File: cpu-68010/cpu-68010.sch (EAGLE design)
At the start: 47 parts, among them IC10 74HC30D, IC11 74HC30D, IC12 74HC85D, IC13 MAX232, IC6 74HC00D, IC7 74HCT154DW, IC8 74HC04D, IC9 74HC148D, X1 FABC96R

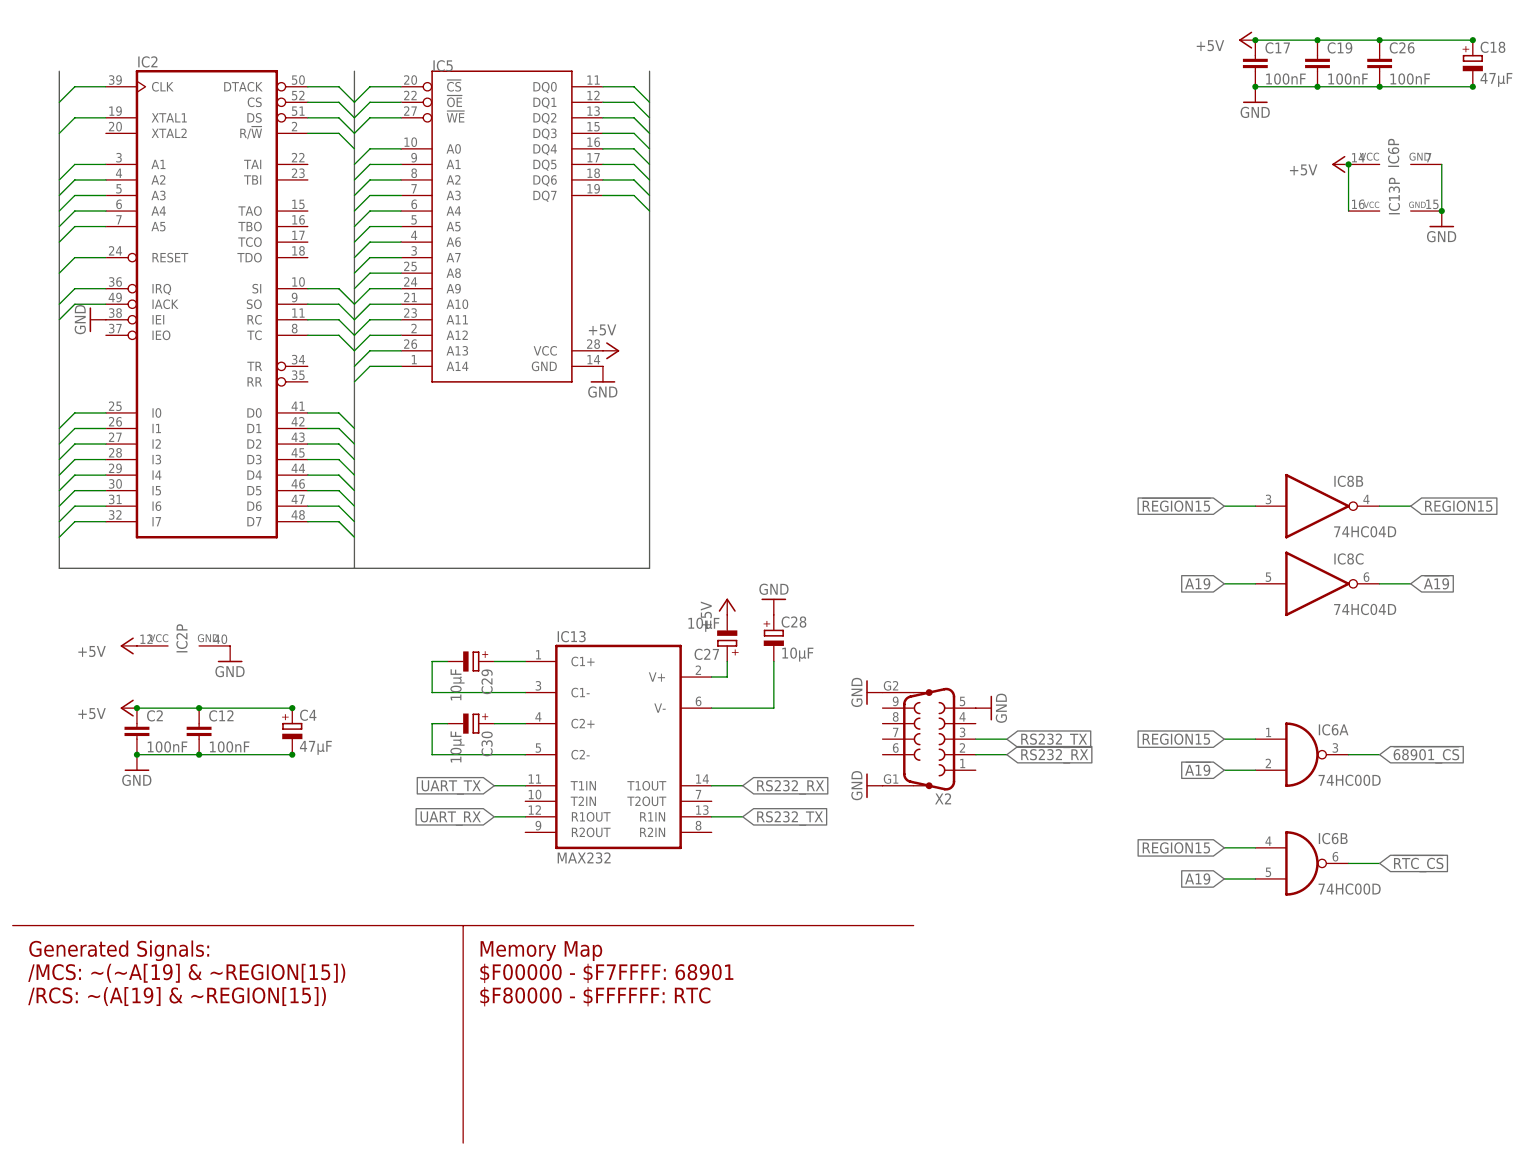
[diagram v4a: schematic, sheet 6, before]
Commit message: removed multifunction peripheral; to be replaced with 68564
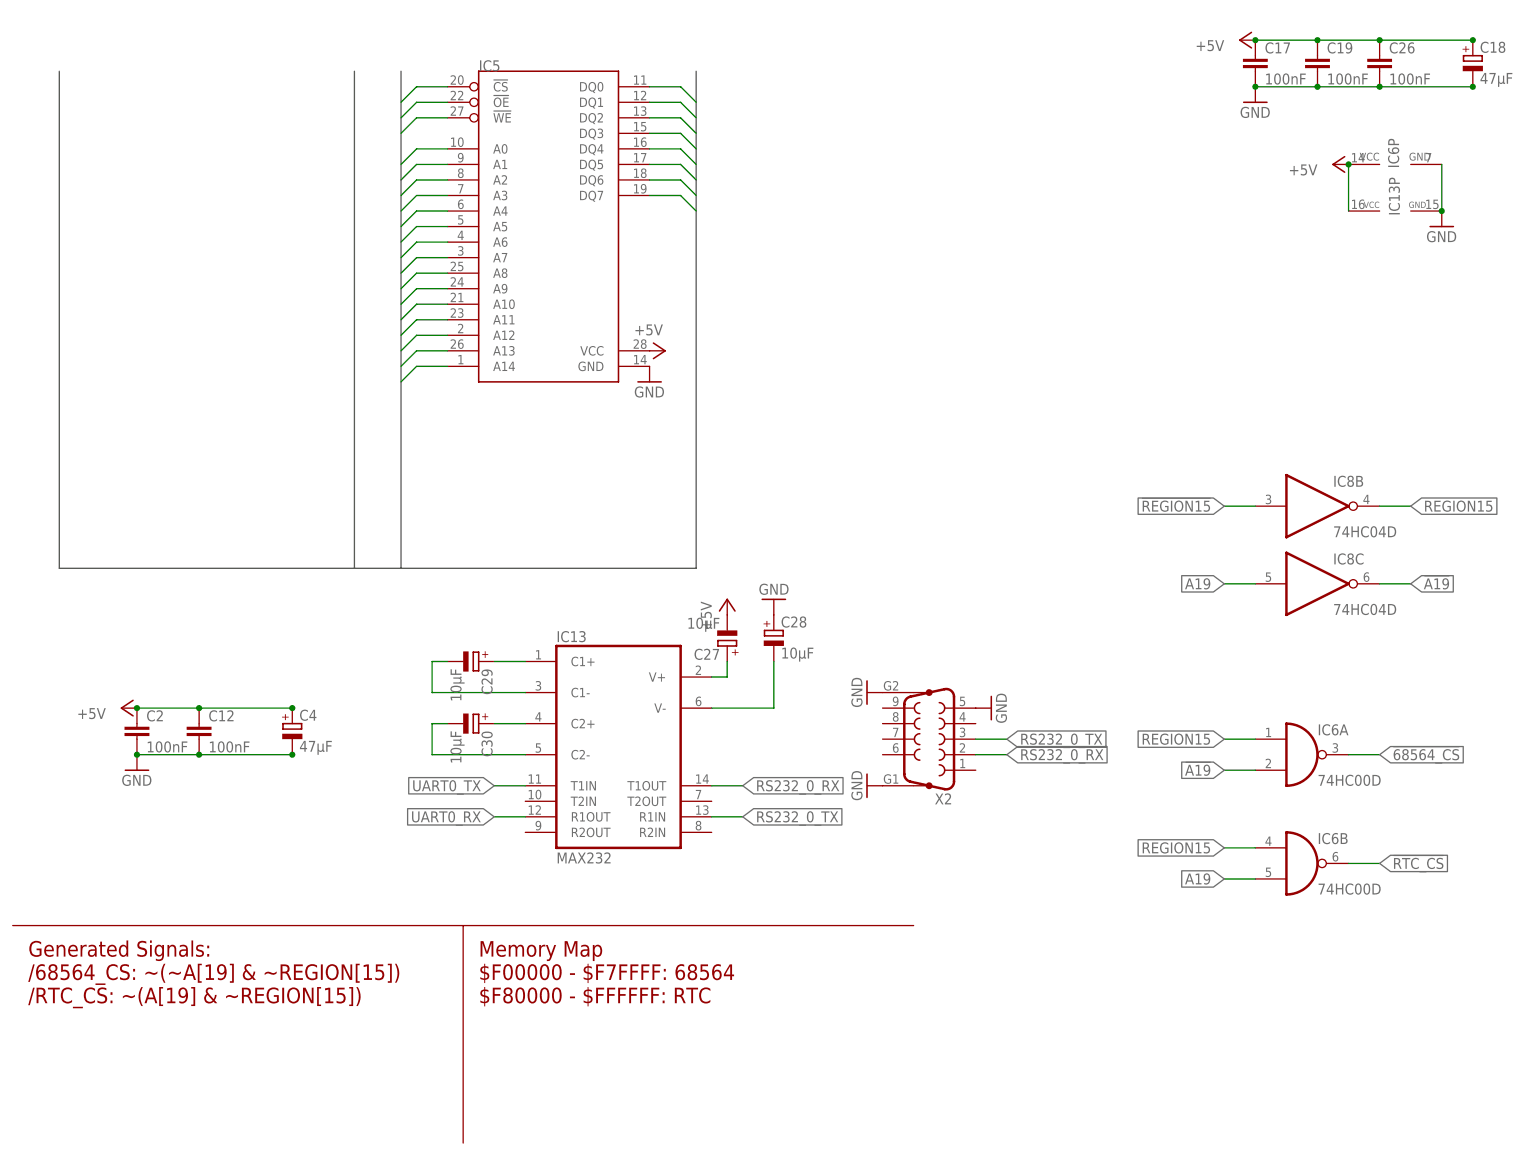
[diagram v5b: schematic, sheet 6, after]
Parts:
- removed IC2: (no value), 68komputer:MC68901FN-SOC
- removed R1: 10k, rcl:R-EU_R2012
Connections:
- net RS232_RX renamed RS232_0_RX
- net RS232_TX renamed RS232_0_TX
- removed net !68901_CS: IC2G$1.CS, IC6A.O
- removed net !68901_DTACK: IC10A.I0, IC2G$1.DTACK, R1.1
- removed net !68901_IACK: IC2G$1.IACK
- removed net !68901_IRQ: IC2G$1.IRQ, IC9A.6
- removed net GPIO0: IC2G$1.I0
- removed net GPIO1: IC2G$1.I1
- removed net GPIO2: IC2G$1.I2
- removed net GPIO3: IC2G$1.I3
- removed net GPIO4: IC2G$1.I4
- removed net GPIO5: IC2G$1.I5
- removed net GPIO6: IC2G$1.I6
- removed net GPIO7: IC2G$1.I7
- removed net UART_CLK: IC2G$1.RC, IC2G$1.TC
- removed net UART_RX: IC13G$1.R1OUT, IC2G$1.SI
- removed net UART_TX: IC13G$1.T1IN, IC2G$1.SO
- new net !68564_CS: IC6A.O
- new net !68564_DTACK: IC10A.I1
- new net !68564_IRQ: IC9A.6
- new net UART0_RX: IC13G$1.R1OUT
- new net UART0_TX: IC13G$1.T1IN
- net !EXT_DTACK: now also IC10A.I0; no longer IC10A.I1
- net !LDS: no longer IC2G$1.DS
- net !RESET: no longer IC2G$1.RESET
- net +5V: no longer IC2P.VCC, R1.2
- net A1: no longer IC2G$1.A1
- net A2: no longer IC2G$1.A2
- net A3: no longer IC2G$1.A3
- net A4: no longer IC2G$1.A4
- net A5: no longer IC2G$1.A5
- net CLK: no longer IC2G$1.CLK, IC2G$1.XTAL1
- net D0: no longer IC2G$1.D0
- net D1: no longer IC2G$1.D1
- net D2: no longer IC2G$1.D2
- net D3: no longer IC2G$1.D3
- net D4: no longer IC2G$1.D4
- net D5: no longer IC2G$1.D5
- net D6: no longer IC2G$1.D6
- net D7: no longer IC2G$1.D7
- net GND: no longer IC2G$1.IEI, IC2P.GND
- net R!W!: no longer IC2G$1.R/!W
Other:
- note added: "Generated Signals: /68564_CS: ~(~A[19] & ~REGION[15]) /RTC_CS: ~(A[19] & ~REGION[15])"
- note added: "Memory Map $F00000 - $F7FFFF: 68564 $F80000 - $FFFFFF: RTC"
- note removed: "Generated Signals: /MCS: ~(~A[19] & ~REGION[15]) /RCS: ~(A[19] & ~REGION[15])"
- note removed: "Memory Map $F00000 - $F7FFFF: 68901 $F80000 - $FFFFFF: RTC"
- moved on the sheet: IC5

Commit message: added 68681 DUART
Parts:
- added C31, C32: 30pF, rcl:C-EUC0805
- added IC2: (no value), 68komputer:MC68681PLCC44-SOCKET
- added LED1, LED2, LED3, LED4, LED5, LED6, LED7, LED8: GRN, led:LEDCHIPLED_1206
- added Q1: 3.6864MHz, crystal:CRYSTALHC49S
- added R1, R10, R11, R2, R3, R4, R5, R6: 680R, rcl:R-EU_M0805
- added X3: (no value), con-subd:F09HP
- IC3, IC4: device 68komputer:SST39SF0X0PDIP-32 -> 68komputer:SST39SF0X0PDIP32
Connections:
- removed net !68564_CS: IC6A.O
- removed net !68564_DTACK: IC10A.I1
- removed net !68564_IRQ: IC9A.6
- new net !68681_CS: IC2.!CS, IC6A.O
- new net !68681_DTACK: IC10A.I1, IC2.!DTACK
- new net !68681_IRQ: IC2.!INTR, IC9A.6
- new net !68681_IRQACK: IC2.!IACK
- new net 68681_XTAL1: C31.1, IC2.X1/CLK, Q1.2
- new net 68681_XTAL2: C32.2, IC2.X2, Q1.1
- new net GPIO_IN0: IC2.IP0
- new net GPIO_IN1: IC2.IP1
- new net GPIO_IN2: IC2.IP2
- new net GPIO_IN3: IC2.IP3
- new net GPIO_IN4: IC2.IP4
- new net GPIO_IN5: IC2.IP5
- new net GPIO_OUT0: IC2.OP0, R4.1
- new net GPIO_OUT1: IC2.OP1, R3.1
- new net GPIO_OUT2: IC2.OP2, R2.1
- new net GPIO_OUT3: IC2.OP3, R1.1
- new net GPIO_OUT4: IC2.OP4, R11.1
- new net GPIO_OUT5: IC2.OP5, R10.1
- new net GPIO_OUT6: IC2.OP6, R6.1
- new net GPIO_OUT7: IC2.OP7, R5.1
- new net N$10: LED1.A, R1.2
- new net N$11: LED2.A, R2.2
- new net N$12: LED1.C, LED2.C
- new net N$13: LED5.A, R3.2
- new net N$14: LED6.A, R4.2
- new net N$15: LED3.C, LED4.C, LED5.C, LED6.C, LED7.C, LED8.C
- new net N$16: LED7.A, R5.2
- new net N$17: LED8.A, R6.2
- new net N$7: LED3.A, R10.2
- new net N$8: LED4.A, R11.2
- new net RS232_1_RX: IC13G$1.T2OUT, X3.2
- new net RS232_1_TX: IC13G$1.R2IN, X3.3
- new net UART1_RX: IC13G$1.R2OUT, IC2.RXDB
- new net UART1_TX: IC13G$1.T2IN, IC2.TXDB
- net !RESET: now also IC2.!RESET
- net +5V: now also IC2.VCC
- net A1: now also IC2.A1
- net A2: now also IC2.A2
- net A3: now also IC2.A3
- net A4: now also IC2.A4
- net D0: now also IC2.D0
- net D1: now also IC2.D1
- net D2: now also IC2.D2
- net D3: now also IC2.D3
- net D4: now also IC2.D4
- net D5: now also IC2.D5
- net D6: now also IC2.D6
- net D7: now also IC2.D7
- net GND: now also C31.2, C32.1, IC2.GND, X3.5, X3.G1, X3.G2
- net R!W!: now also IC2.R/!W
- net UART0_RX: now also IC2.RXDA
- net UART0_TX: now also IC2.TXDA
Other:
- note added: "Generated Signals: /68681_CS: ~(~A[19] & ~REGION[15]) /RTC_CS: ~(A[19] & ~REGION[15])"
- note added: "Memory Map $F00000 - $F7FFFF: 68681 $F80000 - $FFFFFF: RTC"
- note removed: "Generated Signals: /68564_CS: ~(~A[19] & ~REGION[15]) /RTC_CS: ~(A[19] & ~REGION[15])"
- note removed: "Memory Map $F00000 - $F7FFFF: 68564 $F80000 - $FFFFFF: RTC"
- moved on the sheet: C12, C2, C27, C28, C29, C30, C4, IC13, X2

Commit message: added RAM to board, moved some stuff around
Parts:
- added C33, C35, C36, C37, C38, C39, C40: 100nF, rcl:C-EUC0805
- added C34: 47µF, rcl:CPOL-EUCT6032
- added IC14, IC15, IC16, IC17: (no value), 68komputer:CY62128BSOIC32
- added LED9: GRN, led:LEDCHIPLED_1206
- added R12, R7, R8, R9: 10k, rcl:R-EU_M0805
- added R13: 680R, rcl:R-EU_M0805
- added S1, S2: (no value), switch-omron:10-XX
- IC12: value 74HC85D -> 74HC14D; device 74xx-eu:74HC85D -> 74xx-eu:74HC14D
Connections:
- removed net !ROM_WE: IC3.!WE, IC4.!WE
- new net !A18: IC14.CE2, IC15.CE2, IC16.CE2, IC17.CE2, IC8E.O
- new net !TIMER_IRQ: IC9A.6
- new net N$18: R7.2, S1.S, S1.S1
- new net N$19: LED9.A, R13.2
- new net N$9: R8.2, S2.S, S2.S1
- new net NMI_SW: C37.1, IC12A.I, R12.1, R7.1
- new net R/!W!: IC14.!WE, IC15.!WE, IC16.!WE, IC17.!WE, IC3.!WE, IC4.!WE
- new net RESET_SW: C38.1, IC12C.I, R8.1, R9.1
- net !68681_IRQ: now also IC9A.5; no longer IC9A.6
- net !NMI: now also IC12A.O
- net !OE: now also IC14.!OE, IC15.!OE, IC16.!OE, IC17.!OE
- net !REGION1: now also IC14.!CE1, IC15.!CE1, IC16.!CE1, IC17.!CE1
- net !RESET: now also IC12C.O
- net +5V: now also C33.1, C34.+, C35.1, C36.1, C39.1, C40.1, IC14.VCC, IC15.VCC, IC16.VCC, IC17.VCC, R13.1, S1.P, S1.P1, S2.P, S2.P1; no longer IC9A.5
- net A1: now also IC14.A0, IC15.A0, IC16.A0, IC17.A0
- net A10: now also IC14.A9, IC15.A9, IC16.A9, IC17.A9
- net A11: now also IC14.A10, IC15.A10, IC16.A10, IC17.A10
- net A12: now also IC14.A11, IC15.A11, IC16.A11, IC17.A11
- net A13: now also IC14.A12, IC15.A12, IC16.A12, IC17.A12
- net A14: now also IC14.A13, IC15.A13, IC16.A13, IC17.A13
- net A15: now also IC14.A14, IC15.A14, IC16.A14, IC17.A14
- net A16: now also IC14.A15, IC15.A15, IC16.A15, IC17.A15
- net A17: now also IC14.A16, IC15.A16, IC16.A16, IC17.A16
- net A18: now also IC8E.I
- net A2: now also IC14.A1, IC15.A1, IC16.A1, IC17.A1
- net A3: now also IC14.A2, IC15.A2, IC16.A2, IC17.A2
- net A4: now also IC14.A3, IC15.A3, IC16.A3, IC17.A3
- net A5: now also IC14.A4, IC15.A4, IC16.A4, IC17.A4
- net A6: now also IC14.A5, IC15.A5, IC16.A5, IC17.A5
- net A7: now also IC14.A6, IC15.A6, IC16.A6, IC17.A6
- net A8: now also IC14.A7, IC15.A7, IC16.A7, IC17.A7
- net A9: now also IC14.A8, IC15.A8, IC16.A8, IC17.A8
- net D0: now also IC15.D0, IC17.D0
- net D1: now also IC15.D1, IC17.D1
- net D10: now also IC14.D2, IC16.D2
- net D11: now also IC14.D3, IC16.D3
- net D12: now also IC14.D4, IC16.D4
- net D13: now also IC14.D5, IC16.D5
- net D14: now also IC14.D6, IC16.D6
- net D15: now also IC14.D7, IC16.D7
- net D2: now also IC15.D2, IC17.D2
- net D3: now also IC15.D3, IC17.D3
- net D4: now also IC15.D4, IC17.D4
- net D5: now also IC15.D5, IC17.D5
- net D6: now also IC15.D6, IC17.D6
- net D7: now also IC15.D7, IC17.D7
- net D8: now also IC14.D0, IC16.D0
- net D9: now also IC14.D1, IC16.D1
- net GND: now also C33.2, C34.-, C35.2, C36.2, C37.2, C38.2, C39.2, C40.2, IC14.GND, IC15.GND, IC16.GND, IC17.GND, LED9.C, R12.2, R9.2
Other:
- note added: "High RAM"
- note added: "Low RAM"
- moved on the sheet: C10, C11, C21, C23, C24, C25, C5
